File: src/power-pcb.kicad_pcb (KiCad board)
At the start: 2 copper layers, 95.5 x 80 mm, 7 parts, among them J1 XT60-M, J2 ARD_Terminal, J3 MTR1_Terminal, J4 MTR2_Terminal, J5 ESB_Terminal, U1 L2596S, U2 DTD302-V2

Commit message: Add tracks
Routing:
- net +12V: track 21.9 -> 112.5 mm
- net Net-(J2-Pin_1): track 0.00 -> 75.6 mm
- net GND_BAT_CHK: track 0.00 -> 43.6 mm
- net +15V: track 0.00 -> 39.3 mm
- net GND_LOG: track 0.00 -> 30.4 mm
- net GND_BAT: track 0.00 -> 13.4 mm
- net GND: track 22.0 -> 24.0 mm
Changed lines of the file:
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@@
 			)
 		)
-		(sheetname "Racine")
-		(sheetfile "power-pcb.kicad_sch")
 		(attr through_hole)
 		(fp_rect
@@
 		)
 		(fp_text user "IN -> OUT"
-			(at 18 -8 -90)
-			(unlocked yes)
-			(layer "F.Cu")
+			(at 18 -8 270)
+			(unlocked yes)
+			(layer "F.SilkS")
 			(effects
 				(font
@@
 		)
 		(fp_text user "L2596S"
-			(at 20 -11 -90)
-			(unlocked yes)
-			(layer "F.Cu")
+			(at 20 -11 270)
+			(unlocked yes)
+			(layer "F.SilkS")
 			(effects
 				(font
@@
 			(polygon
 				(pts
-					(xy 238.6 64.35) (xy 240.6 64.35) (xy 240.6 108.85) (xy 238.6 108.85) (xy 238.6 110.85) (xy 219.6 110.85)
-					(xy 219.6 108.85) (xy 217.6 108.85) (xy 217.6 64.35) (xy 219.6 64.35) (xy 219.6 62.35) (xy 238.6 62.35)
+					(xy 237.1 65.85) (xy 240.6 65.85) (xy 240.6 107.35) (xy 237.1 107.35) (xy 237.1 110.85) (xy 221.1 110.85)
+					(xy 221.1 107.35) (xy 217.6 107.35) (xy 217.6 65.85) (xy 221.1 65.85) (xy 221.1 62.35) (xy 237.1 62.35)
 				)
 			)
@@
 			)
 		)
-		(sheetname "Racine")
-		(sheetfile "power-pcb.kicad_sch")
 		(attr through_hole)
 		(fp_rect
@@
 			(layer "Edge.Cuts")
 		)
+		(fp_text user "IN -> OUT"
+			(at 24.5 25.5 0)
+			(unlocked yes)
+			(layer "F.SilkS")
+			(effects
+				(font
+					(size 1.5 1.5)
+					(thickness 0.1875)
+				)
+				(justify left bottom)
+			)
+		)
 		(fp_text user "DTD302-V2"
 			(at 24.5 22.5 0)
@@
 			)
 		)
-		(fp_text user "IN -> OUT"
-			(at 24.5 25.5 0)
-			(unlocked yes)
-			(layer "F.SilkS")
-			(effects
-				(font
-					(size 1.5 1.5)
-					(thickness 0.1875)
-				)
-				(justify left bottom)
+		(fp_text user "${REFERENCE}"
+			(at 6 -10.5 0)
+			(unlocked yes)
+			(layer "F.Fab")
+			(effects
+				(font
+					(size 1 1)
+					(thickness 0.15)
+				)
 			)
 		)
 		(pad "1" thru_hole rect
-			(at 4.15 20.15)
+			(at 11.15 20.15)
 			(size 3 3)
 			(drill 1.5)
@@
 		)
 		(pad "2" thru_hole circle
-			(at 4.15 24.85)
+			(at 11.15 24.85)
 			(size 3 3)
 			(drill 1.5)
@@
 		)
 		(pad "3" thru_hole circle
-			(at 55.85 13.65)
+			(at 48.85 13.65)
 			(size 3 3)
 			(drill 1.5)
@@
 		)
 		(pad "4" thru_hole circle
-			(at 55.85 18.65)
+			(at 48.85 18.65)
 			(size 3 3)
 			(drill 1.5)
@@
 	)
 	(segment
-		(start 230.5325 127.5)
+		(start 224.5 115.5)
+		(end 228.0875 115.5)
+		(width 2.5)
+		(layer "F.Cu")
+		(net 1)
+	)
+	(segment
+		(start 217.31 122.69)
+		(end 224.5 115.5)
+		(width 2.5)
+		(layer "F.Cu")
+		(net 1)
+	)
+	(segment
+		(start 217.31 122.7225)
+		(end 217.31 122.69)
+		(width 2.5)
+		(layer "F.Cu")
+		(net 1)
+	)
+	(segment
+		(start 228.0875 115.5)
 		(end 235.31 122.7225)
-		(width 0.2)
+		(width 2.5)
 		(layer "F.Cu")
 		(net 1)
 	)
 	(segment
-		(start 222.0875 127.5)
-		(end 230.5325 127.5)
-		(width 0.2)
-		(layer "F.Cu")
-		(net 1)
-	)
-	(segment
-		(start 217.31 122.7225)
-		(end 222.0875 127.5)
-		(width 0.2)
-		(layer "F.Cu")
-		(net 1)
-	)
-	(segment
-		(start 214.4125 118)
-		(end 222.9675 118)
-		(width 0.2)
-		(layer "F.Cu")
+		(start 235 131.5)
+		(end 239.5 127)
+		(width 2.5)
+		(layer "F.Cu")
+		(net 2)
+	)
+	(segment
+		(start 194.25 131.5)
+		(end 235 131.5)
+		(width 2.5)
+		(layer "F.Cu")
+		(net 2)
+	)
+	(segment
+		(start 239.5 124)
+		(end 239.6 123.9)
+		(width 2.5)
+		(layer "F.Cu")
+		(net 2)
+	)
+	(segment
+		(start 239.6 123.9)
+		(end 239.6 109.85)
+		(width 2.5)
+		(layer "F.Cu")
+		(net 2)
+	)
+	(segment
+		(start 239.5 127)
+		(end 239.5 124)
+		(width 2.5)
+		(layer "F.Cu")
+		(net 2)
+	)
+	(segment
+		(start 186.25 123.5)
+		(end 194.25 131.5)
+		(width 2.5)
+		(layer "F.Cu")
+		(net 2)
+	)
+	(segment
+		(start 226.7 76.25)
+		(end 227.69 77.24)
+		(width 2.5)
+		(layer "B.Cu")
 		(net 3)
 	)
 	(segment
-		(start 222.9675 118)
+		(start 224.44 125.9725)
+		(end 224.44 126.06)
+		(width 2.5)
+		(layer "B.Cu")
+		(net 3)
+	)
+	(segment
+		(start 227.69 77.24)
 		(end 227.69 122.7225)
-		(width 0.2)
-		(layer "F.Cu")
+		(width 2.5)
+		(layer "B.Cu")
 		(net 3)
 	)
 	(segment
-		(start 209.69 122.7225)
-		(end 214.4125 118)
-		(width 0.2)
-		(layer "F.Cu")
+		(start 216.4675 129.5)
+		(end 209.69 122.7225)
+		(width 2.5)
+		(layer "B.Cu")
 		(net 3)
+	)
+	(segment
+		(start 224.44 126.06)
+		(end 221 129.5)
+		(width 2.5)
+		(layer "B.Cu")
+		(net 3)
+	)
+	(segment
+		(start 227.69 122.7225)
+		(end 224.44 125.9725)
+		(width 2.5)
+		(layer "B.Cu")
+		(net 3)
+	)
+	(segment
+		(start 221 129.5)
+		(end 216.4675 129.5)
+		(width 2.5)
+		(layer "B.Cu")
+		(net 3)
+	)
+	(segment
+		(start 239.6 63.35)
+		(end 226.7 76.25)
+		(width 2.5)
+		(layer "B.Cu")
+		(net 3)
+	)
+	(segment
+		(start 226.7 76.25)
+		(end 202.95 76.25)
+		(width 2.5)
+		(layer "B.Cu")
+		(net 3)
+	)
+	(segment
+		(start 207.52 109.85)
+		(end 218.6 109.85)
+		(width 2.5)
+		(layer "F.Cu")
+		(net 4)
+	)
+	(segment
+		(start 193.87 123.5)
+		(end 207.52 109.85)
+		(width 2.5)
+		(layer "F.Cu")
+		(net 4)
+	)
+	(segment
+		(start 165.25 110.15)
+		(end 153.5 121.9)
+		(width 2.5)
+		(layer "B.Cu")
+		(net 5)
+	)
+	(segment
+		(start 165.25 87.45)
+		(end 165.25 110.15)
+		(width 2.5)
+		(layer "B.Cu")
+		(net 5)
+	)
+	(segment
+		(start 159.03 129.1)
+		(end 164.63 123.5)
+		(width 2.5)
+		(layer "F.Cu")
+		(net 6)
+	)
+	(segment
+		(start 153.5 129.1)
+		(end 159.03 129.1)
+		(width 2.5)
+		(layer "F.Cu")
+		(net 6)
+	)
+	(segment
+		(start 172.25 89.75)
+		(end 172.25 123.5)
+		(width 2.5)
+		(layer "B.Cu")
+		(net 7)
+	)
+	(segment
+		(start 165.25 82.75)
+		(end 172.25 89.75)
+		(width 2.5)
+		(layer "B.Cu")
+		(net 7)
 	)
 	(zone
@@
 		(polygon
 			(pts
-				(xy 147.5 59) (xy 243 58) (xy 243 137.5) (xy 147.5 138.5)
-			)
-		)
+				(xy 147.5 58) (xy 243 58) (xy 243 137.5) (xy 147.5 138.5)
+			)
+		)

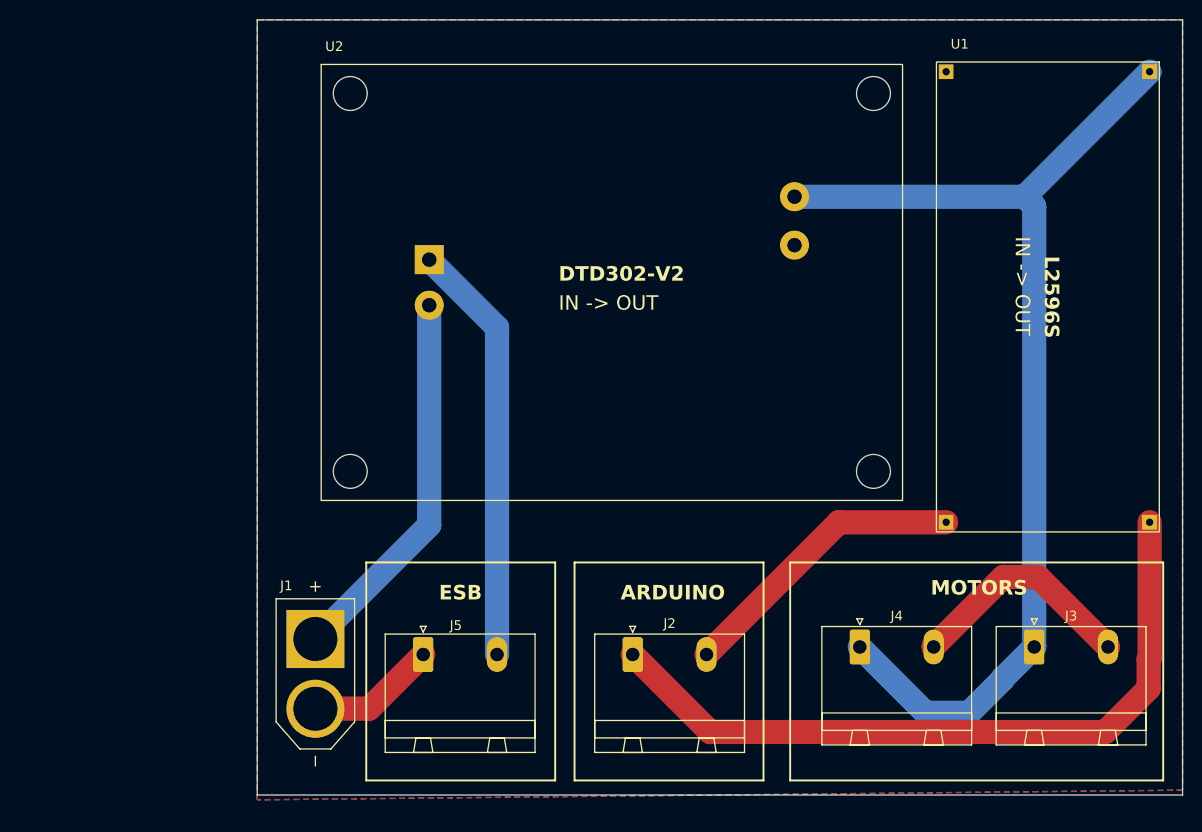
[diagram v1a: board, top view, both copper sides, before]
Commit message: Fix connections order on pwoer connectors
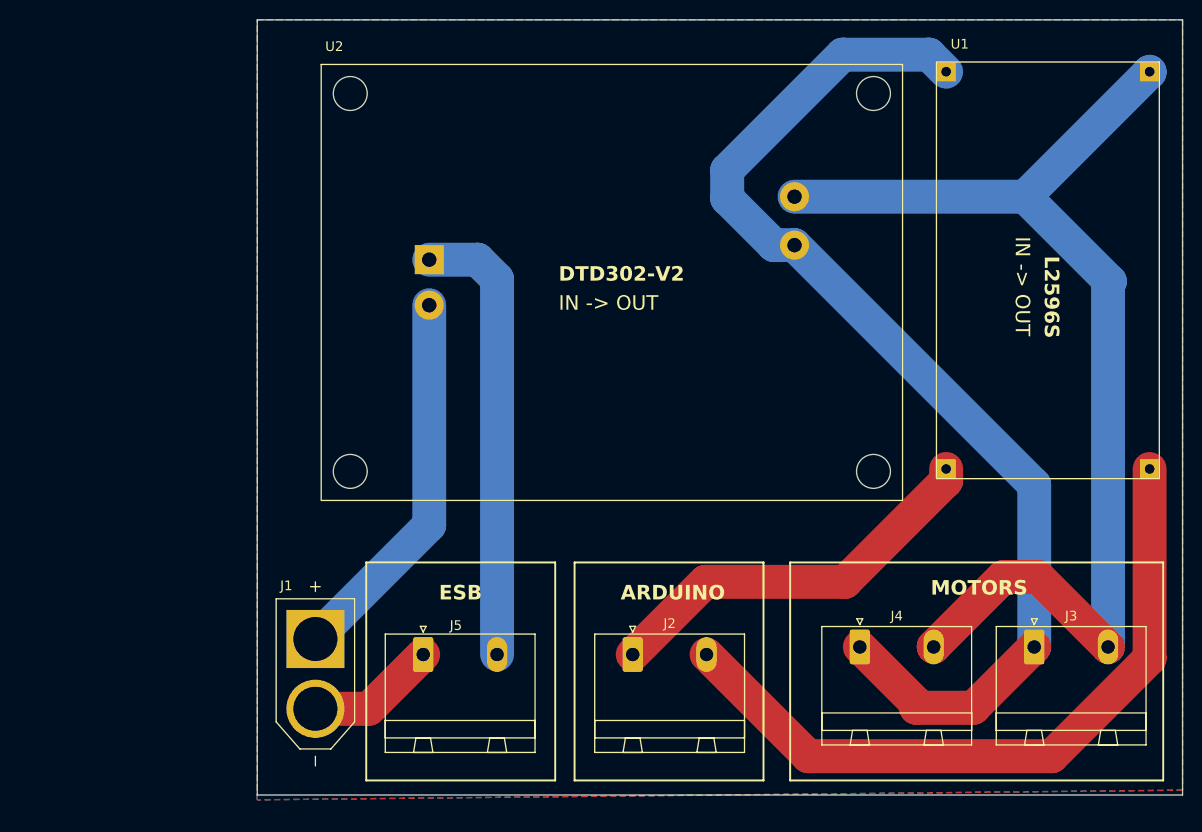
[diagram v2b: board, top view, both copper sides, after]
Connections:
- J2 pad 1: Net-(J2-Pin_1) -> GND_LOG
- J2 pad 2: GND_LOG -> +5V
- J3 pad 1: +12V -> GND
- J3 pad 2: GND -> +12V
- J4 pad 1: +12V -> GND
- J4 pad 2: GND -> +12V
- U1 pad 3: Net-(J2-Pin_1) -> +5V
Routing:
- net GND: track 24.0 -> 115.3 mm
- net Net-(J2-Pin_1): track 75.6 -> 0.00 mm
- net +5V: track 0.00 -> 73.8 mm
- net GND_LOG: track 30.4 -> 41.0 mm
- net +12V: track 112.5 -> 116.2 mm
- net GND_BAT_CHK: track 43.6 -> 46.6 mm

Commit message: Add relay
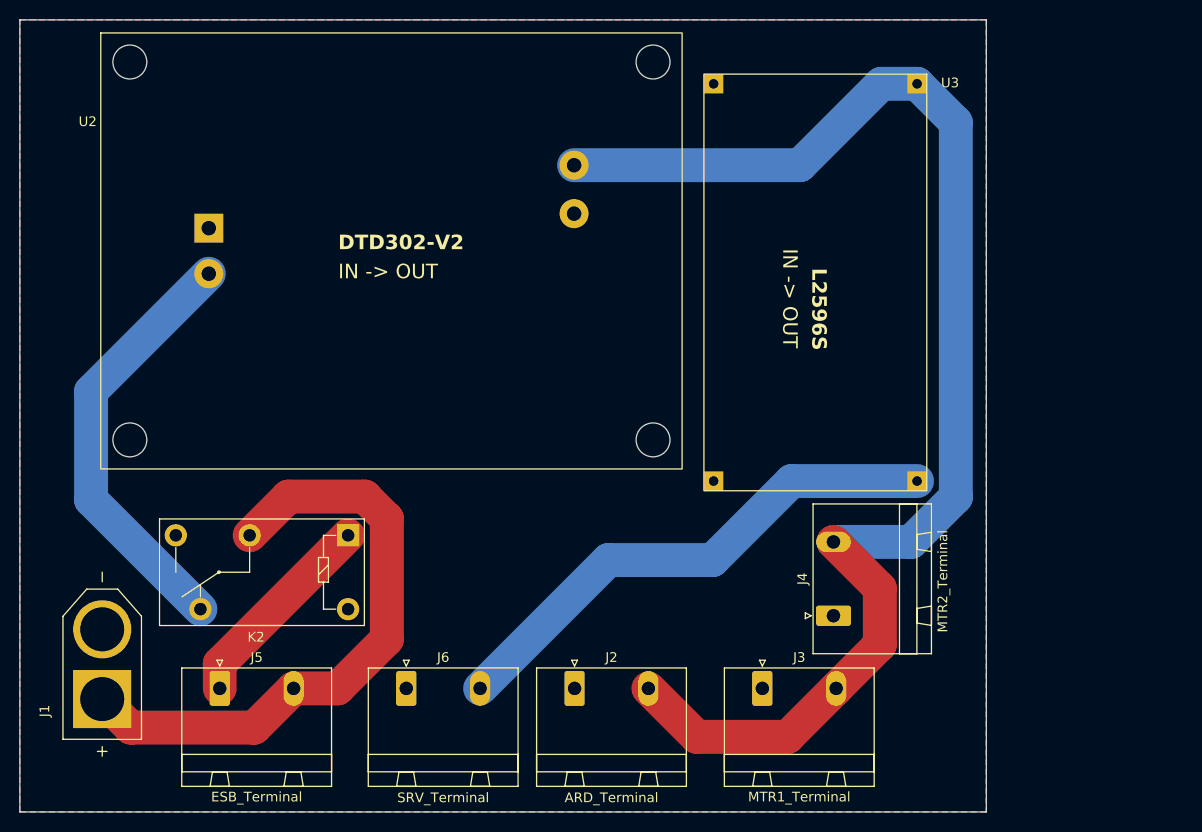
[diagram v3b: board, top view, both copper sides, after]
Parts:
- removed U1: L2596S, Converters_DCDC_Custom:L2596S
- added J6: SRV_Terminal, Connector_Phoenix_GMSTB:PhoenixContact_GMSTBA_2,5_2-G-7,62_1x02_P7.62mm_Horizontal, F.Cu at (162.9, 127.0)
- added K2: G5Q-1, Relay_THT:Relay_SPDT_Omron-G5Q-1, F.Cu at (156.9, 111.2)
- added U3: XL4015, Converters_DCDC_Custom:L2596S, F.Cu at (193.6, 63.6)
- moved J3 28.4 mm to (199.6, 127.0)
- moved U2 23.0 mm to (131.3, 59.4)
- moved J1 22.0 mm to (131.5, 124.5), turned to 90 degrees
- moved J5 21.3 mm to (143.6, 127.0)
- moved J2 6.95 mm to (180.2, 127.0)
- moved J4 4.22 mm to (207.0, 119.5), turned to 90 degrees
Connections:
- J1 pad N: GND_BAT -> GND
- J1 pad P: +15V -> +15V_BATT
- J2 pad 1: GND_LOG -> GND
- J2 pad 2: +5V -> +12V
- J5 pad 1: GND_BAT -> Net-(J5-Pin_1)
- J5 pad 2: GND_BAT_CHK -> +15V_BATT
- U2 pad 1: GND_BAT_CHK -> GND
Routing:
- net GND: track 115.3 -> 0.00 mm
- net +15V_BATT: track 0.00 -> 63.6 mm
- net GND_BAT_CHK: track 46.6 -> 0.00 mm
- net GND_LOG: track 41.0 -> 0.00 mm
- net +12V: track 116.2 -> 140.2 mm
- net Net-(J5-Pin_1): track 0.00 -> 21.3 mm
- net +5V: track 73.8 -> 54.0 mm
- net GND_BAT: track 13.4 -> 0.00 mm
- net +15V: track 39.3 -> 44.3 mm
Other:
- board size 95.5 x 80 mm -> 99.8 x 81.8 mm
- board text removed: "ARDUINO"
- board text removed: "ESB"
- board text removed: "MOTORS"
